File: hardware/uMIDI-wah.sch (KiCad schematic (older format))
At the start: 33 parts, among them IC1 Opamp_Dual_Generic, IC2 L78L09_SOT89, SW1 MMP221, X1 AudioJack3_Switch, X2 Conn_01x08, X3 AudioJack3_Switch

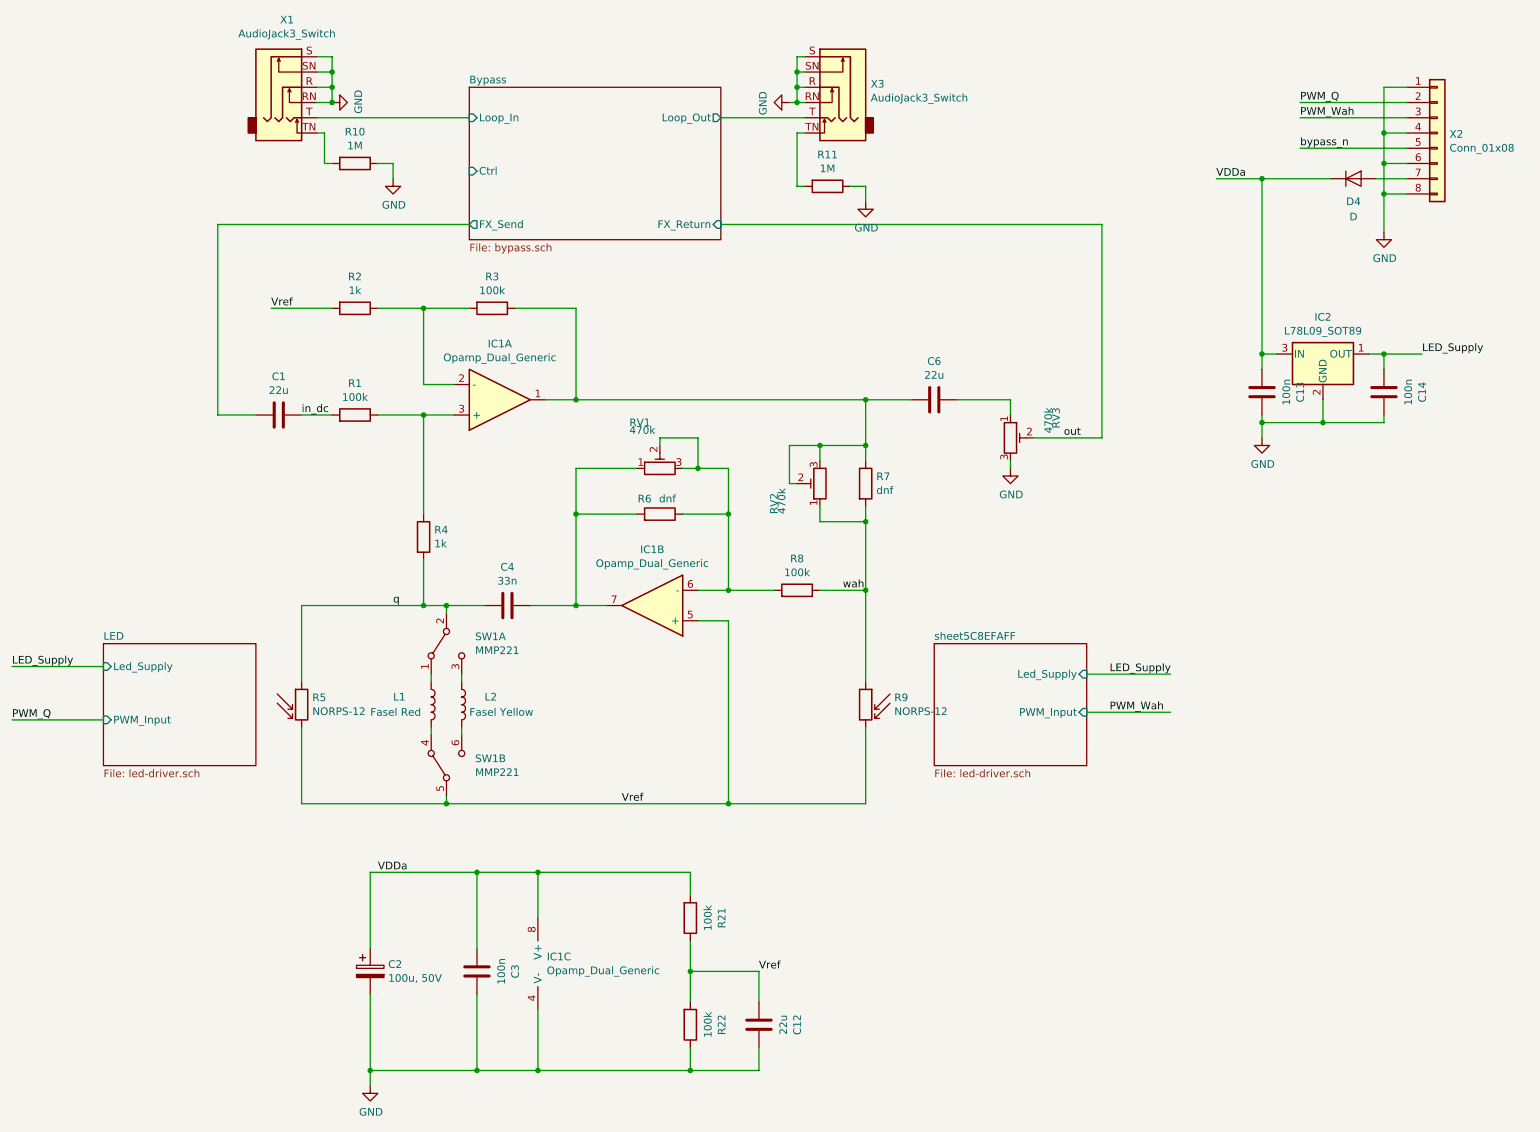
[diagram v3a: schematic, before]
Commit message: Fix footprints
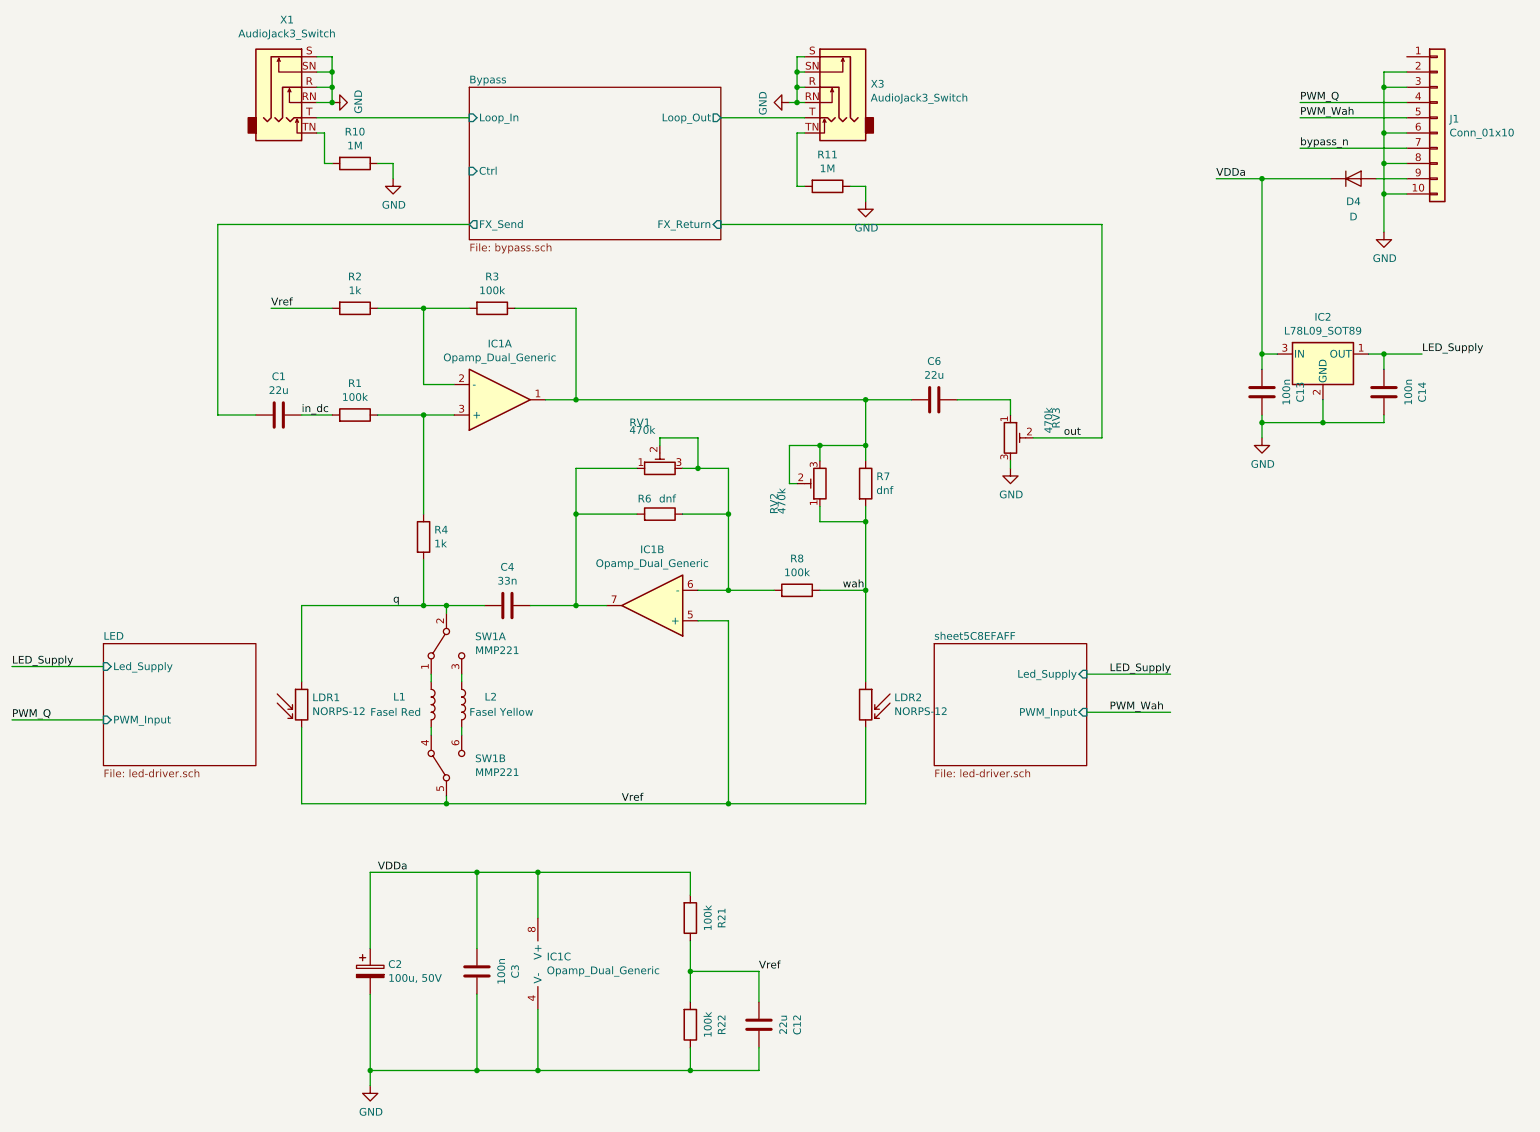
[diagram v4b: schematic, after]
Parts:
- removed X2: Conn_01x08, symbol Connector_Generic:Conn_01x08
- added J1: Conn_01x10, Connector_PinHeader_2.54mm:PinHeader_2x05_P2.54mm_Vertical, symbol Connector_Generic:Conn_01x10
- C1, C12, C13, C14, C3, C4, C6: footprint Capacitors_SMD:C_0805 -> Capacitor_SMD:C_0805_2012Metric_Pad1.15x1.40mm_HandSolder
- R1, R10, R11, R2, R21, R22, R3, R4, R6, R7, R8: footprint Resistors_SMD:R_0805 -> Resistor_SMD:R_0805_2012Metric_Pad1.15x1.40mm_HandSolder
- renumbered R5 to LDR1, R9 to LDR2
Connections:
- net GND: now also J1.10 (Pin_10), J1.2 (Pin_2), J1.3 (Pin_3), J1.6 (Pin_6), J1.8 (Pin_8)
- net PWM_Q: now also J1.4 (Pin_4)
- net PWM_Wah: now also J1.5 (Pin_5)
- net bypass_n: now also J1.7 (Pin_7)
- net at D4.2 (A): now also J1.9 (Pin_9)
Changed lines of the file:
@@
 F 0 "R2" V 3043 2400 50  0000 C CNN
 F 1 "1k" V 3134 2400 50  0000 C CNN
-F 2 "Resistors_SMD:R_0805" V 3180 2400 50  0001 C CNN
+F 2 "Resistor_SMD:R_0805_2012Metric_Pad1.15x1.40mm_HandSolder" V 3180 2400 50  0001 C CNN
 F 3 "" H 3250 2400 50  0001 C CNN
 	1    3250 2400
@@
 F 0 "R1" V 3457 3100 50  0000 C CNN
 F 1 "100k" V 3366 3100 50  0000 C CNN
-F 2 "Resistors_SMD:R_0805" V 3180 3100 50  0001 C CNN
+F 2 "Resistor_SMD:R_0805_2012Metric_Pad1.15x1.40mm_HandSolder" V 3180 3100 50  0001 C CNN
 F 3 "" H 3250 3100 50  0001 C CNN
 	1    3250 3100
@@
 F 0 "R4" H 3770 3946 50  0000 L CNN
 F 1 "1k" H 3770 3855 50  0000 L CNN
-F 2 "Resistors_SMD:R_0805" V 3630 3900 50  0001 C CNN
+F 2 "Resistor_SMD:R_0805_2012Metric_Pad1.15x1.40mm_HandSolder" V 3630 3900 50  0001 C CNN
 F 3 "" H 3700 3900 50  0001 C CNN
 	1    3700 3900
@@
 F 0 "R8" V 6357 4250 50  0000 C CNN
 F 1 "100k" V 6266 4250 50  0000 C CNN
-F 2 "Resistors_SMD:R_0805" V 6080 4250 50  0001 C CNN
+F 2 "Resistor_SMD:R_0805_2012Metric_Pad1.15x1.40mm_HandSolder" V 6080 4250 50  0001 C CNN
 F 3 "" H 6150 4250 50  0001 C CNN
 	1    6150 4250
@@
 F 0 "R7" H 6670 3596 50  0000 L CNN
 F 1 "dnf" H 6670 3505 50  0000 L CNN
-F 2 "Resistors_SMD:R_0805" V 6530 3550 50  0001 C CNN
+F 2 "Resistor_SMD:R_0805_2012Metric_Pad1.15x1.40mm_HandSolder" V 6530 3550 50  0001 C CNN
 F 3 "" H 6600 3550 50  0001 C CNN
 	1    6600 3550
@@
 F 0 "R3" V 3943 2400 50  0000 C CNN
 F 1 "100k" V 4034 2400 50  0000 C CNN
-F 2 "Resistors_SMD:R_0805" V 4080 2400 50  0001 C CNN
+F 2 "Resistor_SMD:R_0805_2012Metric_Pad1.15x1.40mm_HandSolder" V 4080 2400 50  0001 C CNN
 F 3 "" H 4150 2400 50  0001 C CNN
 	1    4150 2400
@@
 F 0 "C6" V 6798 3000 50  0000 C CNN
 F 1 "22u" V 6889 3000 50  0000 C CNN
-F 2 "Capacitors_SMD:C_0805" H 7088 2850 50  0001 C CNN
+F 2 "Capacitor_SMD:C_0805_2012Metric_Pad1.15x1.40mm_HandSolder" H 7088 2850 50  0001 C CNN
 F 3 "" H 7050 3000 50  0001 C CNN
 	1    7050 3000
@@
 F 0 "C4" V 3998 4350 50  0000 C CNN
 F 1 "33n" V 4089 4350 50  0000 C CNN
-F 2 "Capacitors_SMD:C_0805" H 4288 4200 50  0001 C CNN
+F 2 "Capacitor_SMD:C_0805_2012Metric_Pad1.15x1.40mm_HandSolder" H 4288 4200 50  0001 C CNN
 F 3 "" H 4250 4350 50  0001 C CNN
 	1    4250 4350
@@
 F 0 "R6" V 5350 3650 50  0000 C CNN
 F 1 "dnf" V 5350 3800 50  0000 C CNN
-F 2 "Resistors_SMD:R_0805" V 5180 3750 50  0001 C CNN
+F 2 "Resistor_SMD:R_0805_2012Metric_Pad1.15x1.40mm_HandSolder" V 5180 3750 50  0001 C CNN
 F 3 "" H 5250 3750 50  0001 C CNN
 	1    5250 3750
@@
 $EndComp
 $Comp
-L Sensor_Optical:LDR07 R5
+L Sensor_Optical:LDR07 LDR1
 U 1 1 5C8C34D2
 P 2900 5000
-F 0 "R5" H 2970 5046 50  0000 L CNN
+F 0 "LDR1" H 2970 5046 50  0000 L CNN
 F 1 "NORPS-12" H 2970 4955 50  0000 L CNN
 F 2 "umidi-wah:LDR reverse mount" V 3075 5000 50  0001 C CNN
@@
 $EndComp
 $Comp
-L Sensor_Optical:LDR07 R9
+L Sensor_Optical:LDR07 LDR2
 U 1 1 5C8C3558
 P 6600 5000
-F 0 "R9" H 6412 5046 50  0000 R CNN
+F 0 "LDR2" H 6412 5046 50  0000 R CNN
 F 1 "NORPS-12" H 6412 4955 50  0000 R CNN
 F 2 "umidi-wah:LDR reverse mount" V 6775 5000 50  0001 C CNN
@@
 F 0 "C1" V 2498 3100 50  0000 C CNN
 F 1 "22u" V 2589 3100 50  0000 C CNN
-F 2 "Capacitors_SMD:C_0805" H 2788 2950 50  0001 C CNN
+F 2 "Capacitor_SMD:C_0805_2012Metric_Pad1.15x1.40mm_HandSolder" H 2788 2950 50  0001 C CNN
 F 3 "" H 2750 3100 50  0001 C CNN
 	1    2750 3100
@@
 F 0 "R10" V 3043 1450 50  0000 C CNN
 F 1 "1M" V 3134 1450 50  0000 C CNN
-F 2 "Resistors_SMD:R_0805" V 3180 1450 50  0001 C CNN
+F 2 "Resistor_SMD:R_0805_2012Metric_Pad1.15x1.40mm_HandSolder" V 3180 1450 50  0001 C CNN
 F 3 "" H 3250 1450 50  0001 C CNN
 	1    3250 1450
@@
 F 0 "R11" V 6143 1600 50  0000 C CNN
 F 1 "1M" V 6234 1600 50  0000 C CNN
-F 2 "Resistors_SMD:R_0805" V 6280 1600 50  0001 C CNN
+F 2 "Resistor_SMD:R_0805_2012Metric_Pad1.15x1.40mm_HandSolder" V 6280 1600 50  0001 C CNN
 F 3 "" H 6350 1600 50  0001 C CNN
 	1    6350 1600
@@
 	6600 3800 6600 3700
 $Comp
-L Connector_Generic:Conn_01x08 X2
-U 1 1 5CD13F79
-P 10350 1250
-F 0 "X2" H 10430 1242 50  0000 L CNN
-F 1 "Conn_01x08" H 10430 1151 50  0000 L CNN
-F 2 "" H 10350 1250 50  0001 C CNN
-F 3 "~" H 10350 1250 50  0001 C CNN
-	1    10350 1250
-	1    0    0    -1
-$EndComp
-$Comp
 L Device:C C3
 U 1 1 5CD145B7
@@
 F 0 "C3" V 3798 6750 50  0000 C CNN
 F 1 "100n" V 3889 6750 50  0000 C CNN
-F 2 "Capacitors_SMD:C_0805" H 4088 6600 50  0001 C CNN
+F 2 "Capacitor_SMD:C_0805_2012Metric_Pad1.15x1.40mm_HandSolder" H 4088 6600 50  0001 C CNN
 F 3 "" H 4050 6750 50  0001 C CNN
 	1    4050 6750
@@
 F 0 "R21" V 5657 6400 50  0000 C CNN
 F 1 "100k" V 5566 6400 50  0000 C CNN
-F 2 "Resistors_SMD:R_0805" V 5380 6400 50  0001 C CNN
+F 2 "Resistor_SMD:R_0805_2012Metric_Pad1.15x1.40mm_HandSolder" V 5380 6400 50  0001 C CNN
 F 3 "" H 5450 6400 50  0001 C CNN
 	1    5450 6400
@@
 F 0 "R22" V 5657 7100 50  0000 C CNN
 F 1 "100k" V 5566 7100 50  0000 C CNN
-F 2 "Resistors_SMD:R_0805" V 5380 7100 50  0001 C CNN
+F 2 "Resistor_SMD:R_0805_2012Metric_Pad1.15x1.40mm_HandSolder" V 5380 7100 50  0001 C CNN
 F 3 "" H 5450 7100 50  0001 C CNN
 	1    5450 7100
@@
 F 0 "C12" V 5648 7100 50  0000 C CNN
 F 1 "22u" V 5739 7100 50  0000 C CNN
-F 2 "Capacitors_SMD:C_0805" H 5938 6950 50  0001 C CNN
+F 2 "Capacitor_SMD:C_0805_2012Metric_Pad1.15x1.40mm_HandSolder" H 5938 6950 50  0001 C CNN
 F 3 "" H 5900 7100 50  0001 C CNN
 	1    5900 7100
@@
 F 0 "C14" V 9748 2950 50  0000 C CNN
 F 1 "100n" V 9839 2950 50  0000 C CNN
-F 2 "Capacitors_SMD:C_0805" H 10038 2800 50  0001 C CNN
+F 2 "Capacitor_SMD:C_0805_2012Metric_Pad1.15x1.40mm_HandSolder" H 10038 2800 50  0001 C CNN
 F 3 "" H 10000 2950 50  0001 C CNN
 	1    10000 2950
@@
 F 0 "C13" V 8948 2950 50  0000 C CNN
 F 1 "100n" V 9039 2950 50  0000 C CNN
-F 2 "Capacitors_SMD:C_0805" H 9238 2800 50  0001 C CNN
+F 2 "Capacitor_SMD:C_0805_2012Metric_Pad1.15x1.40mm_HandSolder" H 9238 2800 50  0001 C CNN
 F 3 "" H 9200 2950 50  0001 C CNN
 	1    9200 2950
@@
 	8900 1550 9200 1550
 Connection ~ 9200 1550
+$Comp
+L Connector_Generic:Conn_01x10 J1
+U 1 1 5CE0940C
+P 10350 1150
+F 0 "J1" H 10430 1142 50  0000 L CNN
+F 1 "Conn_01x10" H 10430 1051 50  0000 L CNN
+F 2 "Connector_PinHeader_2.54mm:PinHeader_2x05_P2.54mm_Vertical" H 10350 1150 50  0001 C CNN
+F 3 "https://de.rs-online.com/web/p/leiterplatten-header/1216784/" H 10350 1150 50  0001 C CNN
+F 4 "RS" H 10350 1150 50  0001 C CNN "Supplier"
+F 5 "121-6784" H 10350 1150 50  0001 C CNN "Supplier Part Number"
+F 6 "https://de.rs-online.com/web/p/leiterplatten-header/1216784/" H 10350 1150 50  0001 C CNN "Supplier Link"
+F 7 "Wuerth" H 10350 1150 50  0001 C CNN "Manufacturer"
+F 8 "61201021621" H 10350 1150 50  0001 C CNN "Manufacturer Part Number"
+	1    10350 1150
+	1    0    0    -1
+$EndComp
+Wire Wire Line
+	10150 850  10000 850
+Wire Wire Line
+	10000 850  10000 950
+Connection ~ 10000 950
 $EndSCHEMATC

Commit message: Complete initial placement
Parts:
- R10, R11: value 1M -> 100M
- renumbered J1 to X4
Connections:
- net at SW1.6 (C): now also L2.1; no longer L2.2
- net at SW1.3 (C): now also L2.2; no longer L2.1
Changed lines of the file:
@@
 P 3250 1450
 F 0 "R10" V 3043 1450 50  0000 C CNN
-F 1 "1M" V 3134 1450 50  0000 C CNN
+F 1 "100M" V 3134 1450 50  0000 C CNN
 F 2 "Resistor_SMD:R_0805_2012Metric_Pad1.15x1.40mm_HandSolder" V 3180 1450 50  0001 C CNN
 F 3 "" H 3250 1450 50  0001 C CNN
@@
 P 6350 1600
 F 0 "R11" V 6143 1600 50  0000 C CNN
-F 1 "1M" V 6234 1600 50  0000 C CNN
+F 1 "100M" V 6234 1600 50  0000 C CNN
 F 2 "Resistor_SMD:R_0805_2012Metric_Pad1.15x1.40mm_HandSolder" V 6280 1600 50  0001 C CNN
 F 3 "" H 6350 1600 50  0001 C CNN
@@
 F 3 "~" H 3950 5000 50  0001 C CNN
 	1    3950 5000
-	1    0    0    -1
+	1    0    0    1
 $EndComp
 Wire Wire Line
@@
 Connection ~ 9200 1550
 $Comp
-L Connector_Generic:Conn_01x10 J1
+L Connector_Generic:Conn_01x10 X4
 U 1 1 5CE0940C
 P 10350 1150
-F 0 "J1" H 10430 1142 50  0000 L CNN
+F 0 "X4" H 10430 1142 50  0000 L CNN
 F 1 "Conn_01x10" H 10430 1051 50  0000 L CNN
 F 2 "Connector_PinHeader_2.54mm:PinHeader_2x05_P2.54mm_Vertical" H 10350 1150 50  0001 C CNN
@@
 	10000 850  10000 950
 Connection ~ 10000 950
+Wire Wire Line
+	4000 1500 3650 1500
+Text Label 3650 1500 0    50   ~ 0
+bypass_n
 $EndSCHEMATC
